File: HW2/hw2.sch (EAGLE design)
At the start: 23 parts, among them J1 USB-MINIB-5PUSB-MINIB-2SUPPORT, SW3 1825232-1PUSH_BUTTON_2SUPPORT

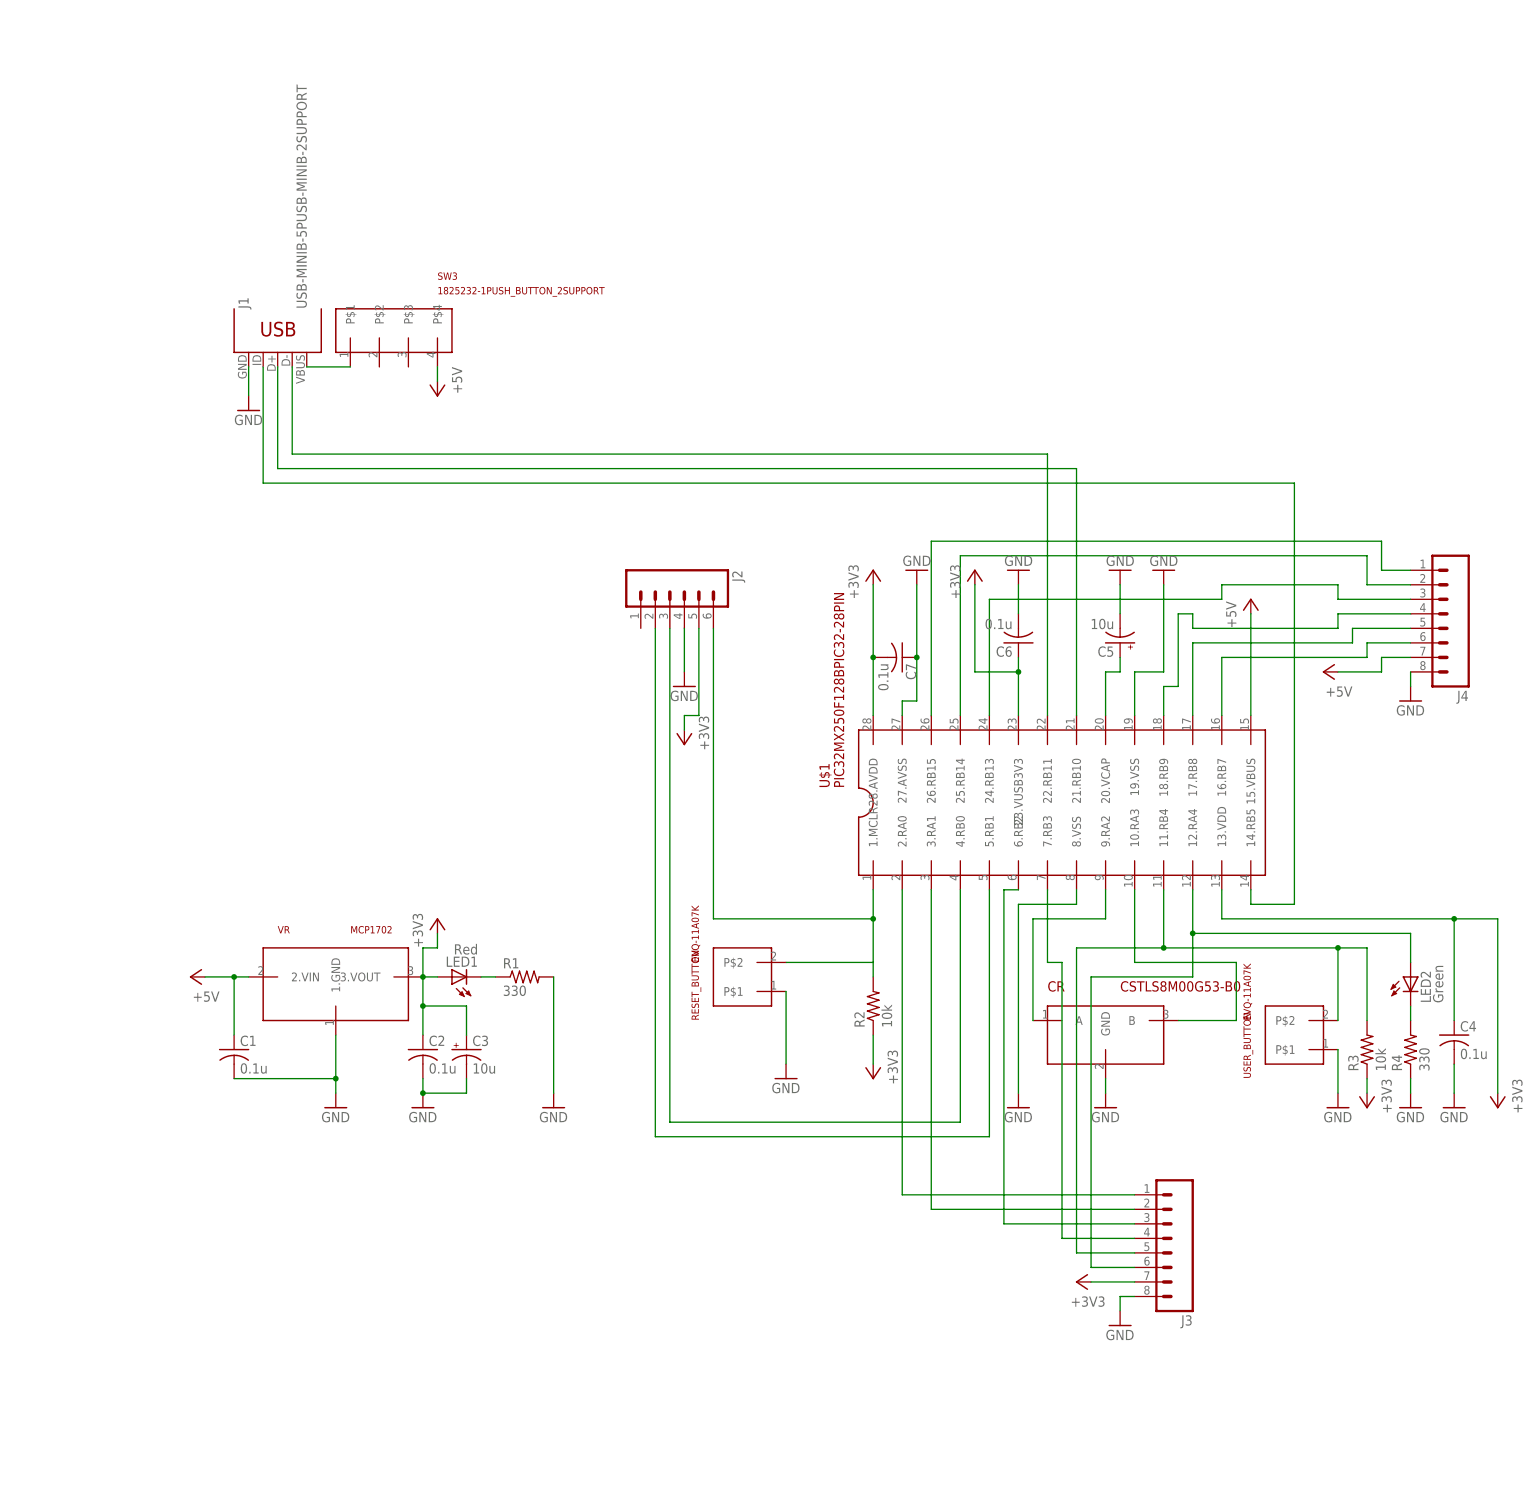
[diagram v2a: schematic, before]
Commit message: Board layout drawn, top and bottom
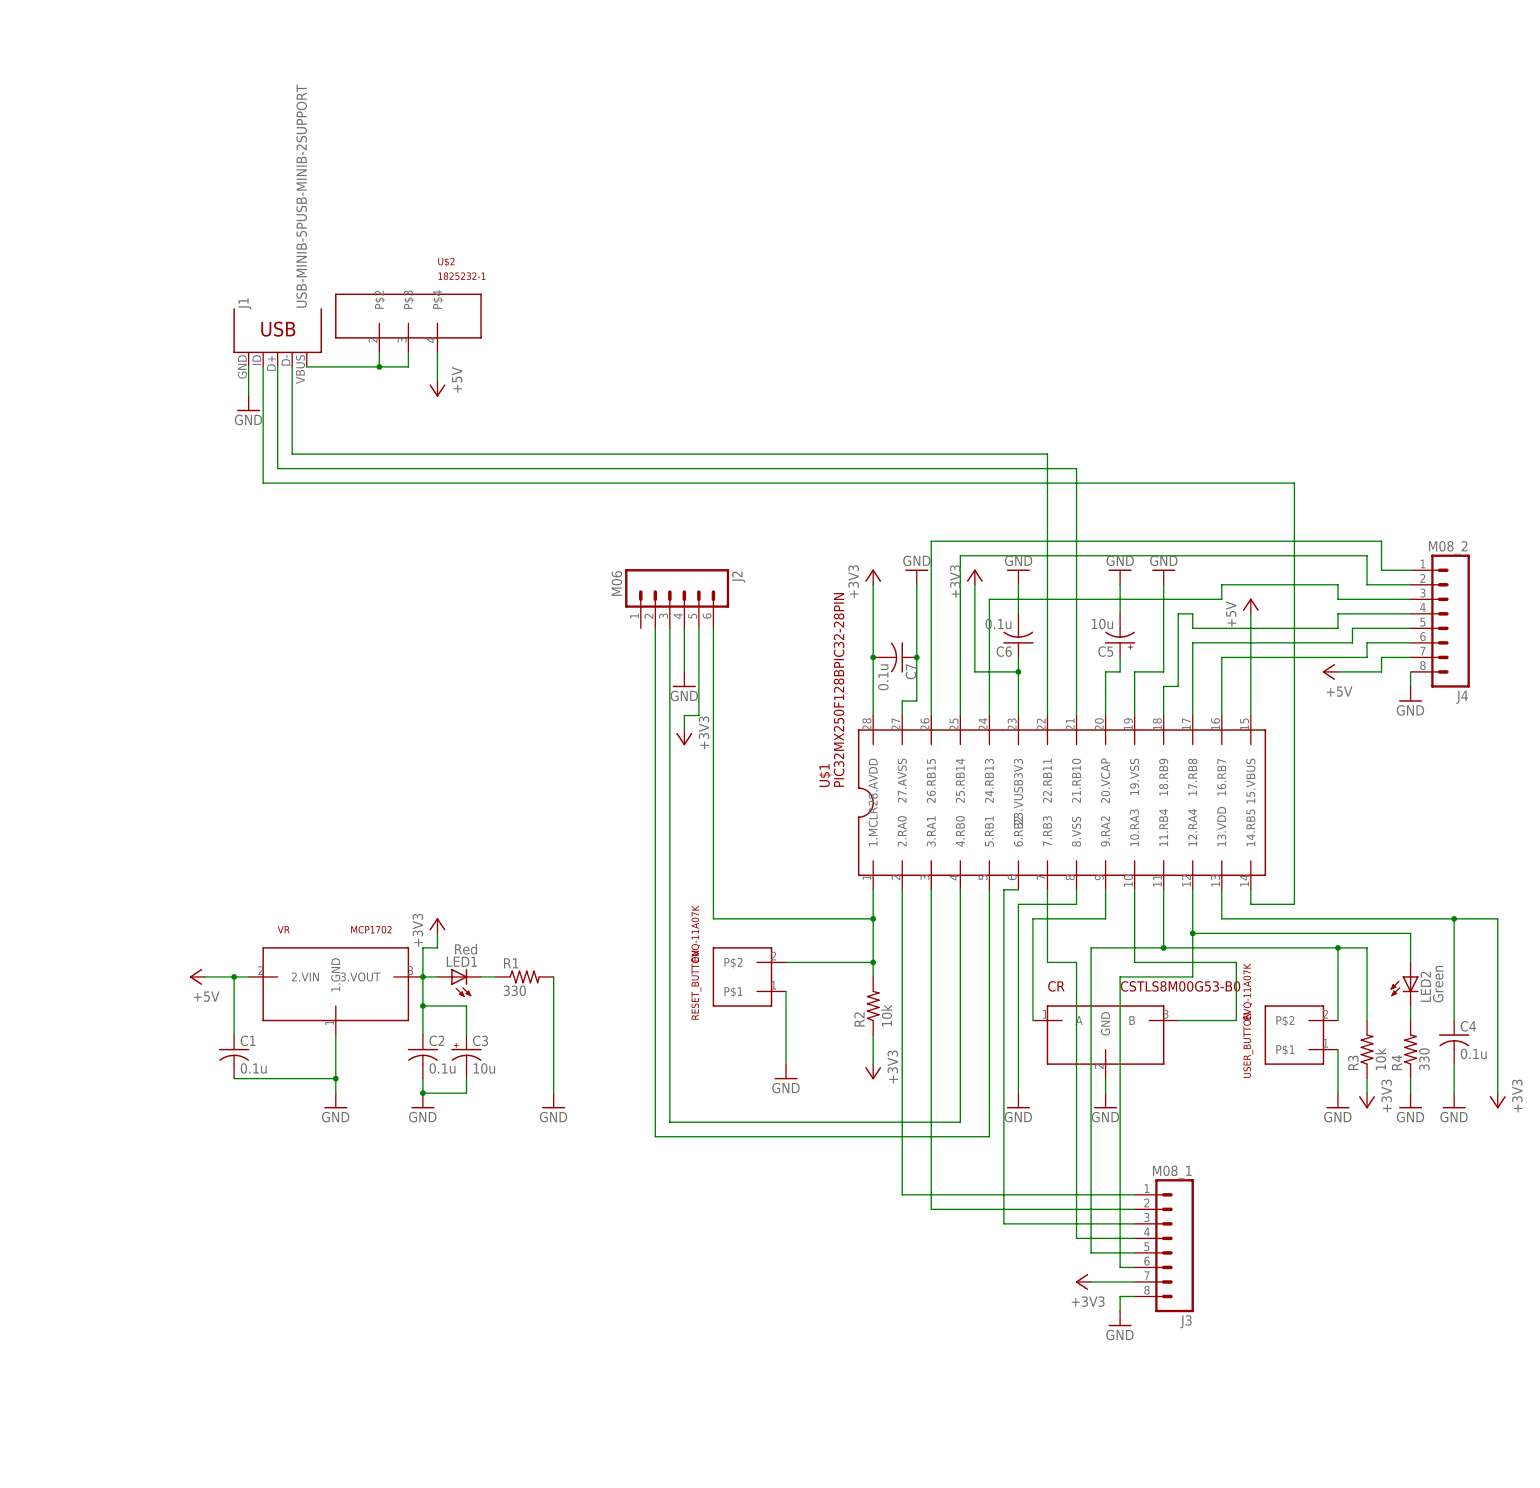
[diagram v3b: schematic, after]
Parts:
- removed SW3: 1825232-1PUSH_BUTTON_2SUPPORT, hw2:1825232-1PUSH_BUTTON_2SUPPORT
- added U$2: 1825232-1, hw2:1825232-1
- J2: value (none) -> M06
- J3: value (none) -> M08_1
- J4: value (none) -> M08_2
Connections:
- net +5V: now also U$2.P$4; no longer SW3.P$4
- net N$4: now also U$2.P$2, U$2.P$3; no longer SW3.P$1
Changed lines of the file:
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@@
 <part name="VR" library="hw2" deviceset="MCP1702" device=""/>
 <part name="J1" library="hw2" deviceset="USB-MINIB-5P" device="USB-MINIB-2SUPPORT"/>
-<part name="J2" library="hw2" deviceset="M06" device="SILK_FEMALE_PTH"/>
+<part name="J2" library="hw2" deviceset="M06" device="SILK_FEMALE_PTH" value="M06"/>
 <part name="GND1" library="hw2" deviceset="GND" device=""/>
 <part name="GND2" library="hw2" deviceset="GND" device=""/>
@@
 <part name="GND8" library="hw2" deviceset="GND" device=""/>
 <part name="+3V1" library="hw2" deviceset="+3V3" device=""/>
-<part name="SW3" library="hw2" deviceset="1825232-1" device="PUSH_BUTTON_2SUPPORT"/>
 <part name="RESET_BUTTON" library="hw2" deviceset="EVQ-11A07K" device=""/>
 <part name="P+3" library="hw2" deviceset="+5V" device=""/>
@@
 <part name="+3V7" library="hw2" deviceset="+3V3" device=""/>
 <part name="GND15" library="hw2" deviceset="GND" device=""/>
-<part name="J3" library="hw2" deviceset="M08" device=""/>
-<part name="J4" library="hw2" deviceset="M08" device=""/>
+<part name="J3" library="hw2" deviceset="M08" device="" value="M08_1"/>
+<part name="J4" library="hw2" deviceset="M08" device="" value="M08_2"/>
 <part name="+3V8" library="hw2" deviceset="+3V3" device=""/>
 <part name="GND16" library="hw2" deviceset="GND" device=""/>
 <part name="P+4" library="hw2" deviceset="+5V" device=""/>
 <part name="GND17" library="hw2" deviceset="GND" device=""/>
+<part name="U$2" library="hw2" deviceset="1825232-1" device=""/>
 </parts>
 <sheets>
@@
 <instance part="GND8" gate="1" x="-111.76" y="-53.34"/>
 <instance part="+3V1" gate="G$1" x="-109.22" y="-20.32"/>
-<instance part="SW3" gate="G$1" x="-116.84" y="81.28"/>
 <instance part="RESET_BUTTON" gate="G$1" x="-53.34" y="-30.48" rot="R90"/>
 <instance part="P+3" gate="1" x="33.02" y="35.56"/>
@@
 <instance part="P+4" gate="1" x="45.72" y="22.86" rot="R90"/>
 <instance part="GND17" gate="1" x="60.96" y="17.78"/>
+<instance part="U$2" gate="G$1" x="-114.3" y="83.82"/>
 </instances>
 <busses>
@@
 </segment>
 <segment>
-<pinref part="SW3" gate="G$1" pin="P$4"/>
 <pinref part="P+1" gate="1" pin="+5V"/>
-<wire x1="-109.22" y1="76.2" x2="-109.22" y2="73.66" width="0.1524" layer="91"/>
+<wire x1="-109.22" y1="73.66" x2="-109.22" y2="78.74" width="0.1524" layer="91"/>
+<pinref part="U$2" gate="G$1" pin="P$4"/>
 </segment>
 <segment>
@@
 <net name="N$7" class="0">
 <segment>
-<pinref part="RESET_BUTTON" gate="G$1" pin="P$2"/>
-<wire x1="-33.02" y1="-27.94" x2="-48.26" y2="-27.94" width="0.1524" layer="91"/>
 <pinref part="R2" gate="G$1" pin="2"/>
-<wire x1="-33.02" y1="-30.48" x2="-33.02" y2="-27.94" width="0.1524" layer="91"/>
 <pinref part="U$1" gate="G$1" pin="1.MCLR"/>
 <wire x1="-60.96" y1="-20.32" x2="-33.02" y2="-20.32" width="0.1524" layer="91"/>
@@
 <pinref part="J2" gate="G$1" pin="6"/>
 <wire x1="-60.96" y1="-20.32" x2="-60.96" y2="30.48" width="0.1524" layer="91"/>
+<wire x1="-33.02" y1="-30.48" x2="-33.02" y2="-27.94" width="0.1524" layer="91"/>
+<junction x="-33.02" y="-20.32"/>
+<pinref part="RESET_BUTTON" gate="G$1" pin="P$2"/>
 <wire x1="-33.02" y1="-27.94" x2="-33.02" y2="-20.32" width="0.1524" layer="91"/>
-<junction x="-33.02" y="-20.32"/>
+<wire x1="-48.26" y1="-27.94" x2="-33.02" y2="-27.94" width="0.1524" layer="91"/>
+<junction x="-33.02" y="-27.94"/>
 </segment>
 </net>
 <net name="N$4" class="0">
 <segment>
-<pinref part="SW3" gate="G$1" pin="P$1"/>
 <pinref part="J1" gate="G$1" pin="VBUS"/>
-<wire x1="-132.08" y1="76.2" x2="-124.46" y2="76.2" width="0.1524" layer="91"/>
+<wire x1="-132.08" y1="76.2" x2="-119.38" y2="76.2" width="0.1524" layer="91"/>
+<pinref part="U$2" gate="G$1" pin="P$2"/>
+<wire x1="-119.38" y1="76.2" x2="-119.38" y2="78.74" width="0.1524" layer="91"/>
+<pinref part="U$2" gate="G$1" pin="P$3"/>
+<wire x1="-119.38" y1="76.2" x2="-114.3" y2="76.2" width="0.1524" layer="91"/>
+<wire x1="-114.3" y1="76.2" x2="-114.3" y2="78.74" width="0.1524" layer="91"/>
+<junction x="-119.38" y="76.2"/>
 </segment>
 </net>
@@
 <junction x="48.26" y="-25.4"/>
 <junction x="17.78" y="-25.4"/>
-<wire x1="17.78" y1="-25.4" x2="2.54" y2="-25.4" width="0.1524" layer="91"/>
-<wire x1="2.54" y1="-25.4" x2="2.54" y2="-78.74" width="0.1524" layer="91"/>
+<wire x1="17.78" y1="-25.4" x2="5.08" y2="-25.4" width="0.1524" layer="91"/>
+<wire x1="5.08" y1="-25.4" x2="5.08" y2="-78.74" width="0.1524" layer="91"/>
 <pinref part="J3" gate="G$1" pin="5"/>
-<wire x1="2.54" y1="-78.74" x2="12.7" y2="-78.74" width="0.1524" layer="91"/>
+<wire x1="5.08" y1="-78.74" x2="12.7" y2="-78.74" width="0.1524" layer="91"/>
 </segment>
 </net>
@@
 <wire x1="22.86" y1="-22.86" x2="22.86" y2="-30.48" width="0.1524" layer="91"/>
 <junction x="22.86" y="-22.86"/>
-<wire x1="22.86" y1="-30.48" x2="5.08" y2="-30.48" width="0.1524" layer="91"/>
-<wire x1="5.08" y1="-30.48" x2="5.08" y2="-81.28" width="0.1524" layer="91"/>
+<wire x1="22.86" y1="-30.48" x2="10.16" y2="-30.48" width="0.1524" layer="91"/>
+<wire x1="10.16" y1="-30.48" x2="10.16" y2="-81.28" width="0.1524" layer="91"/>
 <pinref part="J3" gate="G$1" pin="6"/>
-<wire x1="5.08" y1="-81.28" x2="12.7" y2="-81.28" width="0.1524" layer="91"/>
+<wire x1="10.16" y1="-81.28" x2="12.7" y2="-81.28" width="0.1524" layer="91"/>
 </segment>
 </net>
@@
 <pinref part="U$1" gate="G$1" pin="7.RB3"/>
 <wire x1="-2.54" y1="-15.24" x2="-2.54" y2="-27.94" width="0.1524" layer="91"/>
-<wire x1="-2.54" y1="-27.94" x2="0" y2="-27.94" width="0.1524" layer="91"/>
-<wire x1="0" y1="-27.94" x2="0" y2="-76.2" width="0.1524" layer="91"/>
+<wire x1="-2.54" y1="-27.94" x2="2.54" y2="-27.94" width="0.1524" layer="91"/>
+<wire x1="2.54" y1="-27.94" x2="2.54" y2="-76.2" width="0.1524" layer="91"/>
 <pinref part="J3" gate="G$1" pin="4"/>
-<wire x1="0" y1="-76.2" x2="12.7" y2="-76.2" width="0.1524" layer="91"/>
-</segment>
-</net>
+<wire x1="2.54" y1="-76.2" x2="12.7" y2="-76.2" width="0.1524" layer="91"/>
+</segment>
+</net>
